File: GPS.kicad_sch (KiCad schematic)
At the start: 47 parts, among them J101 USB_B_Micro, J102 Conn_01x05, J103 Conn_01x10, U101 AP7361C-10E, U102 AZ1117-3.3, U103 AZ1117-3.3, U104 SMA_CONN, U105 M10578-A2, U106 MCP2562-H-SN, U107 STM32F103C8T6, Y101 8MHz

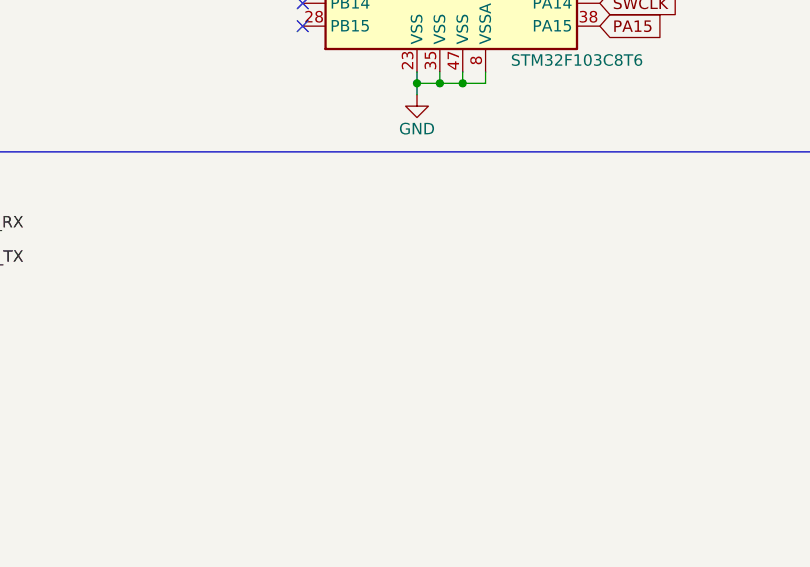
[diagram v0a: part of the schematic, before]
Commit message: Add files via upload
Updated PCB layout with proper RF traces and differential pairs. PCB dimensions are now 70 mm by 70 mm
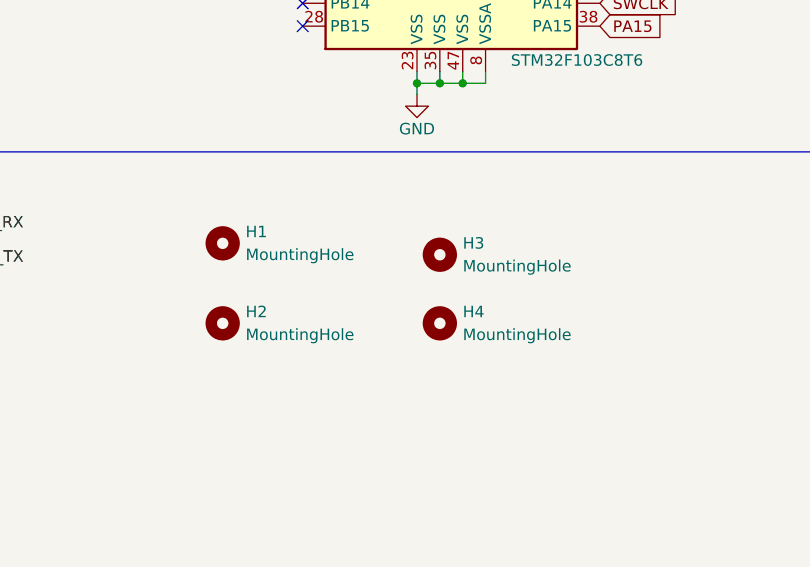
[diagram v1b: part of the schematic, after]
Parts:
- added H1, H2, H3, H4: MountingHole, MountingHole:MountingHole_3.2mm_M3, symbol Mechanical:MountingHole
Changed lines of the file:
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@@
     (pin "1")
+  )
+  (symbol (lib_id "Mechanical:MountingHole") (at 236.22 152.4 0) (unit 1)
+    (in_bom yes) (on_board yes) (fields_autoplaced)
+    (property "Reference" "H3" (id 0) (at 238.76 151.1299 0)
+      (effects (font (size 1.27 1.27)) (justify left))
+    )
+    (property "Value" "MountingHole" (id 1) (at 238.76 153.6699 0)
+      (effects (font (size 1.27 1.27)) (justify left))
+    )
+    (property "Footprint" "MountingHole:MountingHole_3.2mm_M3" (id 2) (at 236.22 152.4 0)
+      (effects (font (size 1.27 1.27)) hide)
+    )
+    (property "Datasheet" "~" (id 3) (at 236.22 152.4 0)
+      (effects (font (size 1.27 1.27)) hide)
+    )
   )
   (symbol (lib_id "Device:LED_Small") (at 86.36 161.29 180) (unit 1)
@@
     (pin "1")
     (pin "2")
+  )
+  (symbol (lib_id "Mechanical:MountingHole") (at 212.09 151.13 0) (unit 1)
+    (in_bom yes) (on_board yes) (fields_autoplaced)
+    (property "Reference" "H1" (id 0) (at 214.63 149.8599 0)
+      (effects (font (size 1.27 1.27)) (justify left))
+    )
+    (property "Value" "MountingHole" (id 1) (at 214.63 152.3999 0)
+      (effects (font (size 1.27 1.27)) (justify left))
+    )
+    (property "Footprint" "MountingHole:MountingHole_3.2mm_M3" (id 2) (at 212.09 151.13 0)
+      (effects (font (size 1.27 1.27)) hide)
+    )
+    (property "Datasheet" "~" (id 3) (at 212.09 151.13 0)
+      (effects (font (size 1.27 1.27)) hide)
+    )
   )
   (symbol (lib_id "Device:C_Small") (at 205.74 27.94 0) (unit 1)
@@
     (pin "1")
   )
+  (symbol (lib_id "Mechanical:MountingHole") (at 212.09 160.02 0) (unit 1)
+    (in_bom yes) (on_board yes) (fields_autoplaced)
+    (property "Reference" "H2" (id 0) (at 214.63 158.7499 0)
+      (effects (font (size 1.27 1.27)) (justify left))
+    )
+    (property "Value" "MountingHole" (id 1) (at 214.63 161.2899 0)
+      (effects (font (size 1.27 1.27)) (justify left))
+    )
+    (property "Footprint" "MountingHole:MountingHole_3.2mm_M3" (id 2) (at 212.09 160.02 0)
+      (effects (font (size 1.27 1.27)) hide)
+    )
+    (property "Datasheet" "~" (id 3) (at 212.09 160.02 0)
+      (effects (font (size 1.27 1.27)) hide)
+    )
+  )
   (symbol (lib_id "Device:C_Small") (at 89.662 135.382 0) (unit 1)
     (in_bom yes) (on_board yes)
@@
     (pin "1")
   )
+  (symbol (lib_id "Mechanical:MountingHole") (at 236.22 160.02 0) (unit 1)
+    (in_bom yes) (on_board yes) (fields_autoplaced)
+    (property "Reference" "H4" (id 0) (at 238.76 158.7499 0)
+      (effects (font (size 1.27 1.27)) (justify left))
+    )
+    (property "Value" "MountingHole" (id 1) (at 238.76 161.2899 0)
+      (effects (font (size 1.27 1.27)) (justify left))
+    )
+    (property "Footprint" "MountingHole:MountingHole_3.2mm_M3" (id 2) (at 236.22 160.02 0)
+      (effects (font (size 1.27 1.27)) hide)
+    )
+    (property "Datasheet" "~" (id 3) (at 236.22 160.02 0)
+      (effects (font (size 1.27 1.27)) hide)
+    )
+  )
   (symbol (lib_id "Device:C_Small") (at 162.814 159.258 0) (unit 1)
     (in_bom yes) (on_board yes)
@@
       (reference "D104") (unit 1) (value "BLUE") (footprint "LED_SMD:LED_0603_1608Metric")
     )
+    (path "/22637260-465e-4536-be27-64a16f9dfac6"
+      (reference "H1") (unit 1) (value "MountingHole") (footprint "MountingHole:MountingHole_3.2mm_M3")
+    )
+    (path "/cad0863a-182b-4740-b420-fb1b7bbe933b"
+      (reference "H2") (unit 1) (value "MountingHole") (footprint "MountingHole:MountingHole_3.2mm_M3")
+    )
+    (path "/18beeed9-acbf-444d-b864-ca8409e12e13"
+      (reference "H3") (unit 1) (value "MountingHole") (footprint "MountingHole:MountingHole_3.2mm_M3")
+    )
+    (path "/ea56028d-b46e-4c3b-9c87-1384286a2695"
+      (reference "H4") (unit 1) (value "MountingHole") (footprint "MountingHole:MountingHole_3.2mm_M3")
+    )
     (path "/ffe75c60-dd70-4e4a-9967-34b4966d7f4d"

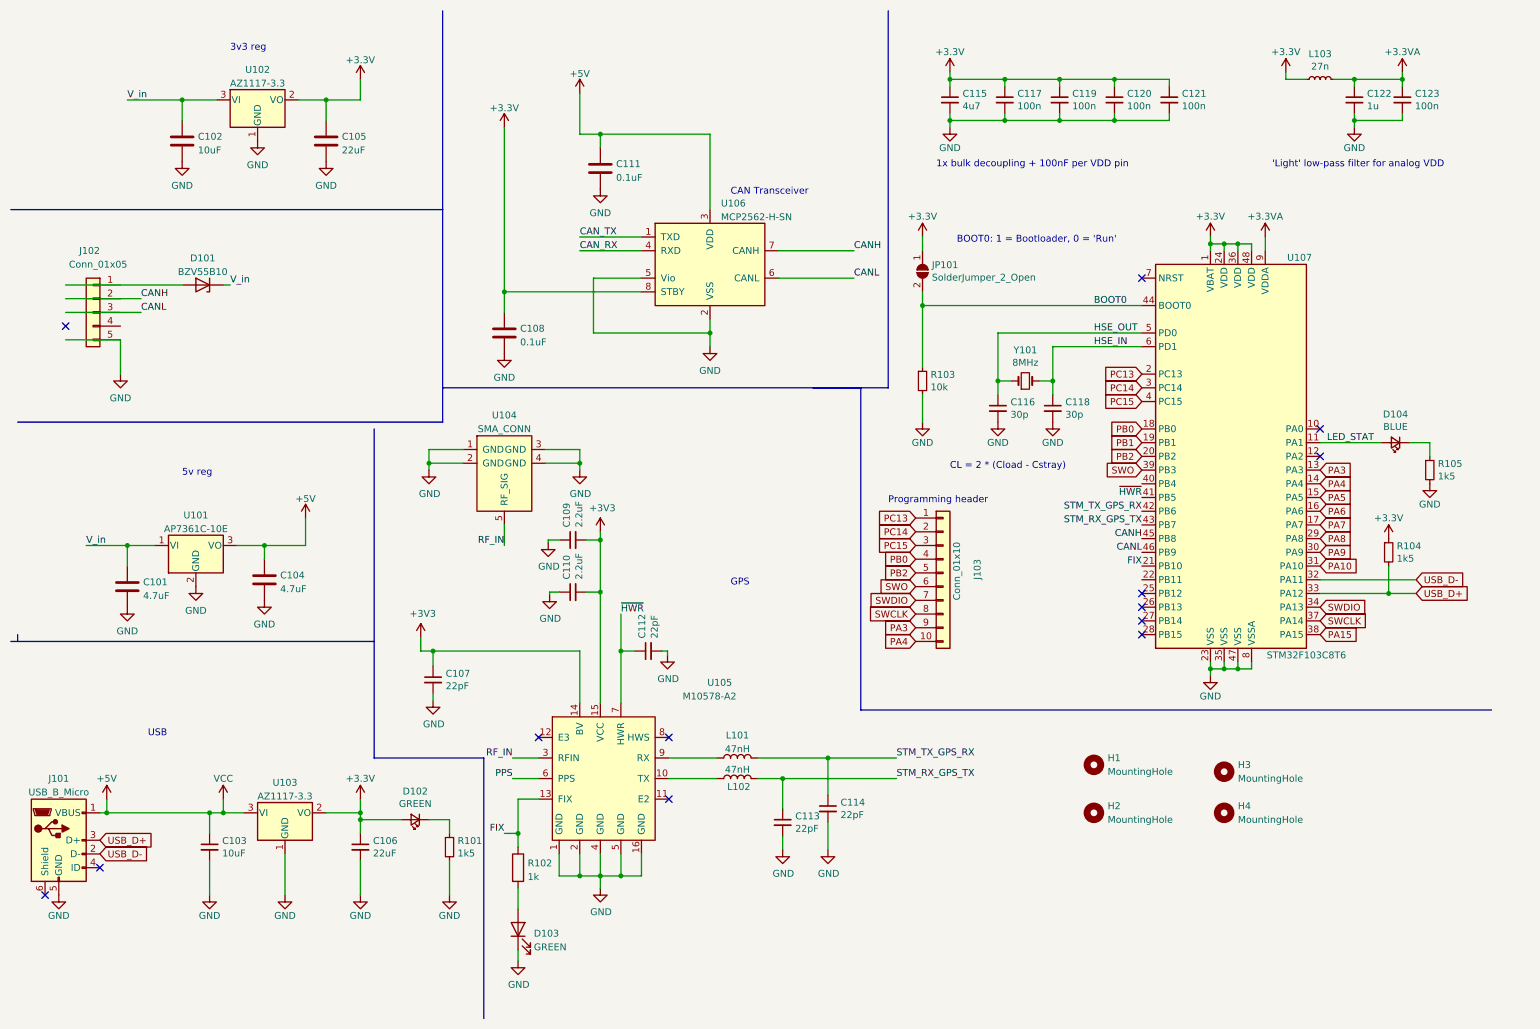
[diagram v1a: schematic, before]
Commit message: made changes for CANH/L and added STM programming header
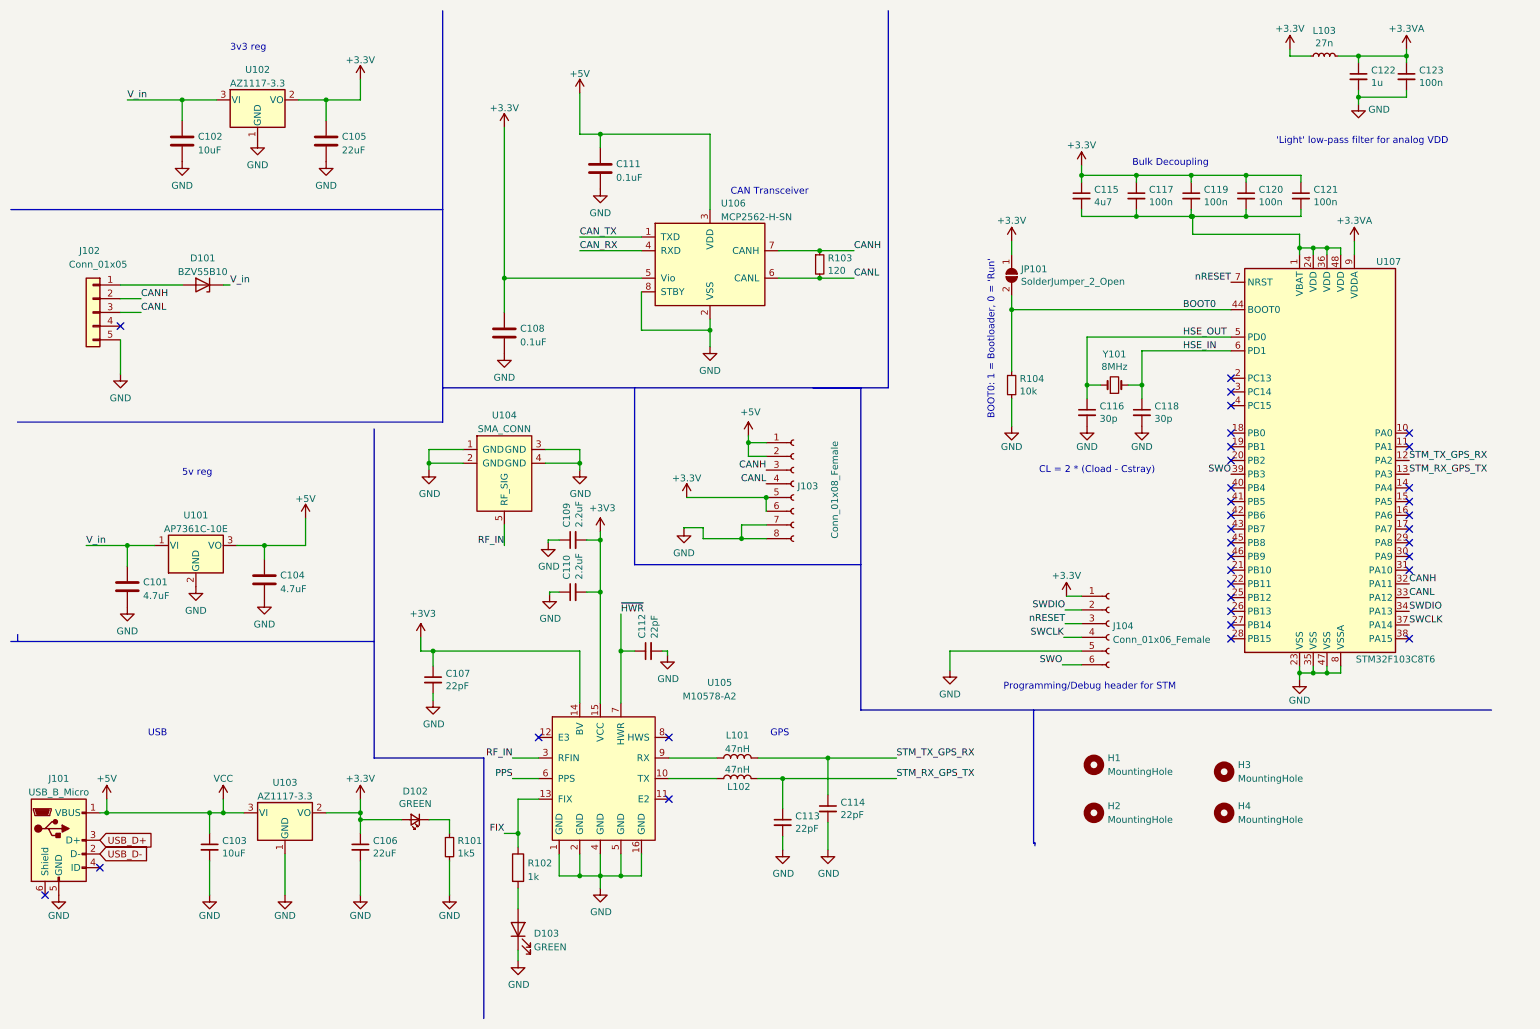
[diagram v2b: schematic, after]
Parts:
- removed D104: BLUE, LED_SMD:LED_0603_1608Metric, symbol Device:LED_Small
- removed J103: Conn_01x10, Connector_PinHeader_1.27mm:PinHeader_1x10_P1.27mm_Horizontal, symbol Connector_Generic:Conn_01x10
- removed R105: 1k5, Resistor_SMD:R_0805_2012Metric, symbol Device:R_Small
- added J103: Conn_01x08_Female, Connector_PinHeader_1.27mm:PinHeader_1x08_P1.27mm_Horizontal, symbol Connector:Conn_01x08_Female
- added J104: Conn_01x06_Female, Connector:Tag-Connect_TC2030-IDC-FP_2x03_P1.27mm_Vertical, symbol Connector:Conn_01x06_Female
- C115, C116, C117, C118, C119, C120, C121, C122, C123: footprint Capacitor_SMD:C_0805_2012Metric -> Capacitor_SMD:C_0805_2012Metric_Pad1.18x1.45mm_HandSolder
- R103: value 10k -> 120
- R104: value 1k5 -> 10k; footprint Resistor_SMD:R_0805_2012Metric -> Resistor_SMD:R_0805_2012Metric_Pad1.20x1.40mm_HandSolder; LCSC Part # C25867 -> C25744
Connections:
- net PA3 is gone; now on net STM_RX_GPS_TX: U107.13 (PA3)
- net +3.3V: now also U106.5 (Vio), J103.5 (Pin_5), J103.6 (Pin_6), J104.1 (Pin_1); no longer R104.1, U106.8 (STBY), U107.1 (VBAT), U107.24 (VDD), U107.36 (VDD), U107.48 (VDD)
- net +5V: now also J103.1 (Pin_1), J103.2 (Pin_2)
- net BOOT0: now also R104.1; no longer R103.1
- net CANH: now also J102.2 (Pin_2), R103.1, U107.32 (PA11), J103.3 (Pin_3); no longer U107.45 (PB8)
- net CANL: now also J102.3 (Pin_3), R103.2, U107.33 (PA12), J103.4 (Pin_4); no longer U107.46 (PB9)
- net FIX: no longer U107.21 (PB10)
- net GND: now also R104.2, U106.8 (STBY), J103.7 (Pin_7), J103.8 (Pin_8), J104.5 (Pin_5); no longer C115.2, C117.2, C119.2, C120.2, C121.2, R103.2, U106.5 (Vio)
- net STM_RX_GPS_TX: no longer U107.43 (PB7)
- net STM_TX_GPS_RX: now also U107.12 (PA2); no longer U107.42 (PB6)
- net SWCLK: now also J104.4 (Pin_4)
- net SWDIO: now also J104.2 (Pin_2)
- net SWO: now also J104.6 (Pin_6)
- net USB_D+: no longer R104.2, U107.33 (PA12)
- net USB_D-: no longer U107.32 (PA11)
- net ~{HWR}: no longer U107.41 (PB5)
- net at D101.2 (A): now also J102.1 (Pin_1)
- net nRESET: now reaches U107.7 (NRST)
- net nRESET: now also J104.3 (Pin_3)
- net LED_STAT: no longer names the net of U107.11 (PA1)
- net PA10: no longer names the net of U107.31 (PA10)
- net PA15: no longer names the net of U107.38 (PA15)
- net PA4: no longer names the net of U107.14 (PA4)
- net PA5: no longer names the net of U107.15 (PA5)
- net PA6: no longer names the net of U107.16 (PA6)
- net PA7: no longer names the net of U107.17 (PA7)
- net PA8: no longer names the net of U107.29 (PA8)
- net PA9: no longer names the net of U107.30 (PA9)
- net PB0: no longer names the net of U107.18 (PB0)
- net PB1: no longer names the net of U107.19 (PB1)
- net PB2: no longer names the net of U107.20 (PB2)
- net PC13: no longer names the net of U107.2 (PC13)
- net PC14: no longer names the net of U107.3 (PC14)
- net PC15: no longer names the net of U107.4 (PC15)
- new net: C115.2, C117.2, C119.2, C120.2, C121.2, U107.1 (VBAT), U107.24 (VDD), U107.36 (VDD), U107.48 (VDD)
- no-connect marks 13 -> 34
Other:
- note added: "Bulk Decoupling"
- note added: "Programming/Debug header for STM"
- note removed: "1x bulk decoupling + 100nF per VDD pin"
- note removed: "Programming header"
